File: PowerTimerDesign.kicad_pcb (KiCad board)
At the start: 2 copper layers, 49.5 x 124.5 mm, 45 parts, among them SW1 0041_9146_3317, SW2 0041_9146_3317, SW3 0041_9146_3317, SW4 0041_9146_3317, U1 NE556, U2 NE556, U3 4082, U4 4082

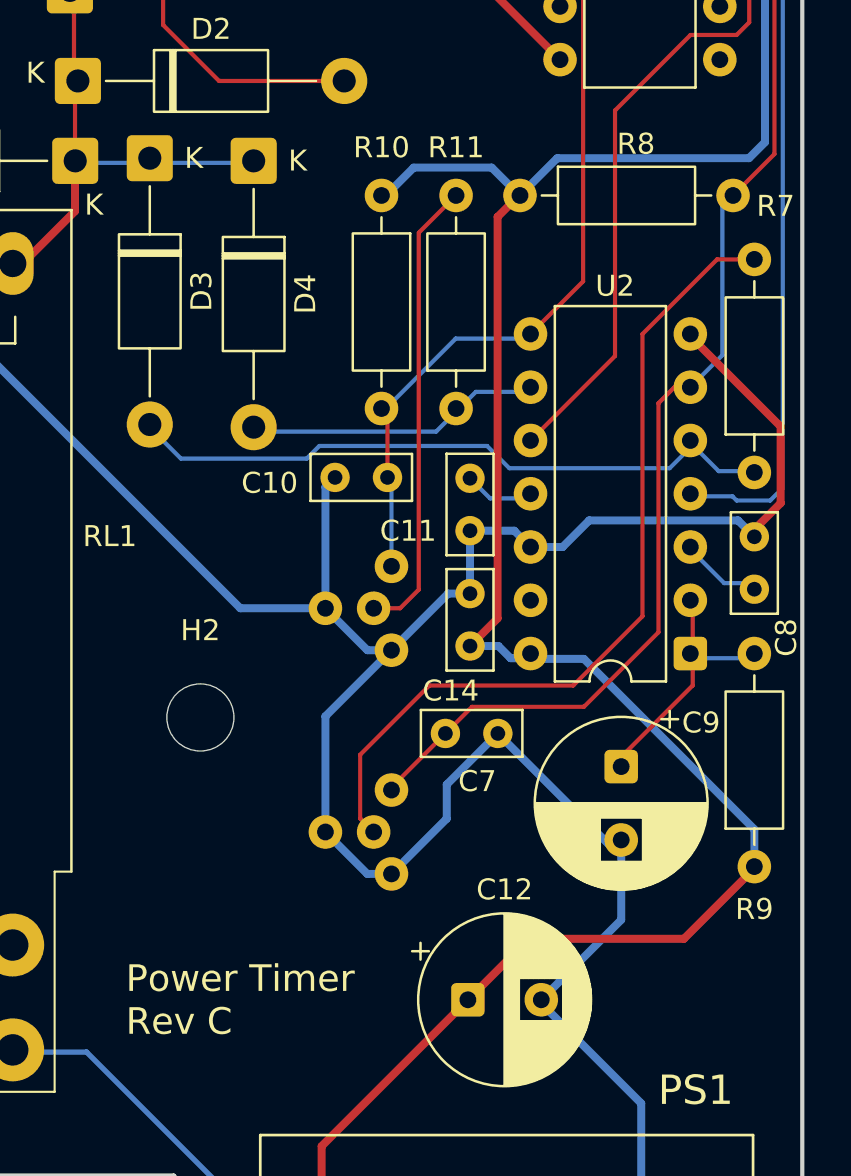
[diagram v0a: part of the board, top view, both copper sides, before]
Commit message: Replaced Rev C design with Rev D
Swapped R10 & R11 Ref Des (they were on the wrong resistor).
Rewired SW3 and SW4 so their functions would be swapped (so on Rev D, the order on the unit is now: Stay On, 1 Hour, 10 Minutes & 5 Minutes)
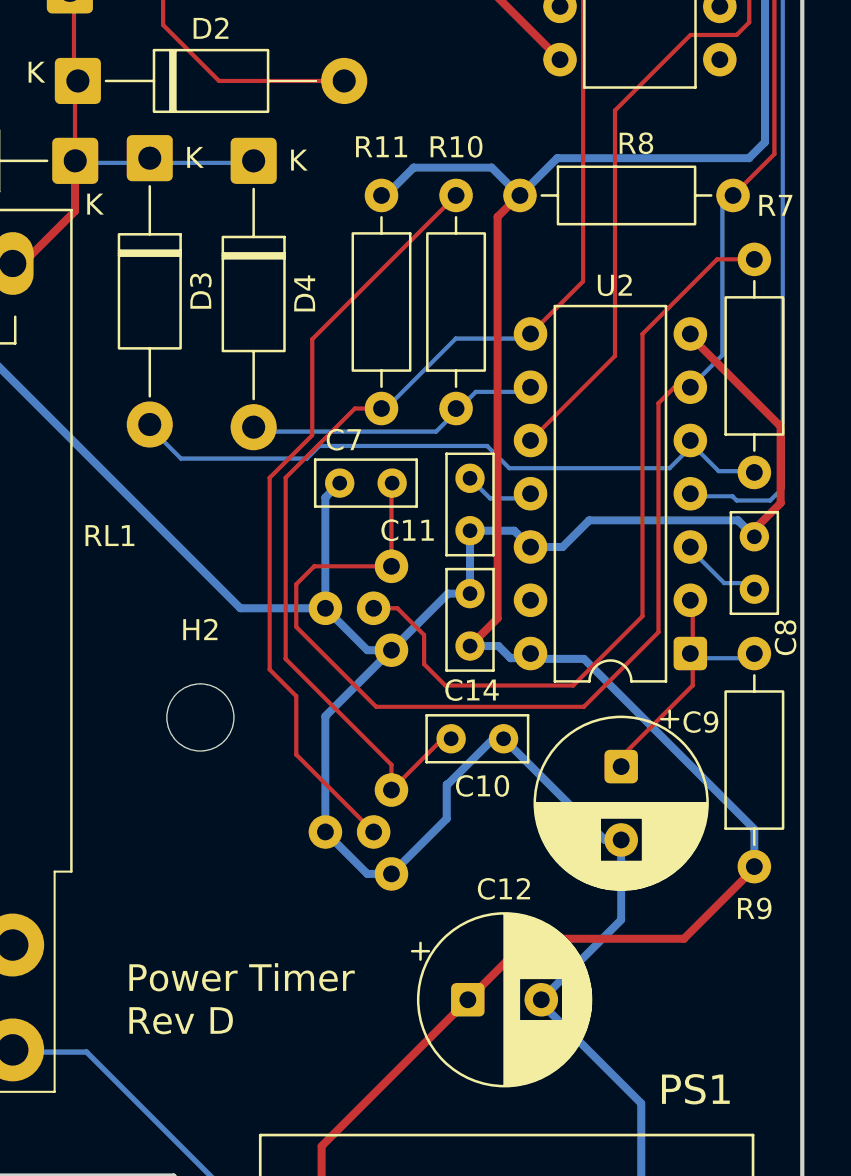
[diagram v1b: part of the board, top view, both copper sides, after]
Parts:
- moved C10 12.8 mm to (83.6, 127.8), turned to 0 degrees
- moved C7 12.2 mm to (80.8, 115.6), turned to 180 degrees
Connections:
- SW3 pad 2: /Timers/SET60 -> /Timers/SETON
- SW3 pad 6: /Timers/LED60 -> /Timers/LEDON
- SW4 pad 2: /Timers/SETON -> /Timers/SET60
- SW4 pad 6: /Timers/LEDON -> /Timers/LED60
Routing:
- net /Timers/SETON: track 70.0 -> 89.3 mm
- net /Timers/SET60: track 88.9 -> 104.2 mm
- net /Timers/LEDON: track 22.1 -> 36.1 mm
- net /Timers/LED60: track 40.4 -> 36.8 mm
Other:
- board text added: "Power Timer Rev D"
- board text removed: "Power Timer Rev C"
